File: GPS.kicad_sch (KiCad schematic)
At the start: 8 parts, among them J10 SMAConn, SW3 GPS_BattCheck, U7 MTK3339

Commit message: cleaner, still needs full checklisting
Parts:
- SW3: footprint Button_Switch_SMD:SW_SPST_B3SL-1002P -> UTSVT_Special:SW_SPST_B3SL-1002P
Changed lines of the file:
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@@
       (effects (font (size 1.27 1.27)) (justify left))
     )
-    (property "Footprint" "Button_Switch_SMD:SW_SPST_B3SL-1002P" (at 95.885 122.555 0)
+    (property "Footprint" "UTSVT_Special:SW_SPST_B3SL-1002P" (at 95.885 122.555 0)
       (effects (font (size 1.27 1.27)) hide)
     )

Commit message: neatening things up
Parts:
- J10: footprint Connector_Coaxial:SMA_Amphenol_132203-12_Horizontal -> UTSVT_Connectors:SMA_Amphenol_132203-12_Horizontal
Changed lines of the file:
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@@
       (effects (font (size 1.27 1.27)) (justify left))
     )
-    (property "Footprint" "Connector_Coaxial:SMA_Amphenol_132203-12_Horizontal" (at 192.405 98.425 0)
+    (property "Footprint" "UTSVT_Connectors:SMA_Amphenol_132203-12_Horizontal" (at 192.405 98.425 0)
       (effects (font (size 1.27 1.27)) hide)
     )

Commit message: bom, gerbers, edge cuts, footprint verification
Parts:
- BT2: P/N (none) -> 3000TR
- J10: P/N (none) -> 132203-12
- R26: P/N (none) -> CR0805-FX-5490ELF
- R27: P/N (none) -> CRCW0805750RFKEAHP
- U7: P/N (none) -> MTK3339
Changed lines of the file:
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@@
       (effects (font (size 1.27 1.27)) hide)
     )
-    (property "Datasheet" "~" (at 131.699 83.185 90)
+    (property "Datasheet" "https://www.mouser.com/datasheet/2/215/3000TR-742873.pdf" (at 131.699 83.185 90)
+      (effects (font (size 1.27 1.27)) hide)
+    )
+    (property "P/N" "3000TR" (at 130.175 83.185 0)
       (effects (font (size 1.27 1.27)) hide)
     )
@@
       (effects (font (size 1.27 1.27)) hide)
     )
-    (property "Datasheet" "~" (at 113.665 107.315 0)
+    (property "Datasheet" "https://www.mouser.com/datasheet/2/427/dcrcwe3-1762152.pdf" (at 113.665 107.315 0)
+      (effects (font (size 1.27 1.27)) hide)
+    )
+    (property "P/N" "CRCW0805750RFKEAHP" (at 113.665 107.315 0)
       (effects (font (size 1.27 1.27)) hide)
     )
@@
       (effects (font (size 1.27 1.27)) hide)
     )
-    (property "Datasheet" " ~" (at 192.405 98.425 0)
+    (property "Datasheet" "https://www.mouser.com/datasheet/2/18/1/amphs06488_1-2259725.pdf" (at 192.405 98.425 0)
+      (effects (font (size 1.27 1.27)) hide)
+    )
+    (property "P/N" "132203-12" (at 192.405 98.425 0)
       (effects (font (size 1.27 1.27)) hide)
     )
@@
     )
     (property "Datasheet" "https://www.mouser.com/ProductDetail/Adafruit/790?qs=sGAEpiMZZMu3sxpa5v1qro3UYtn2%252BmNbf7YcQf0l2Dw%3D" (at 168.275 73.025 0)
+      (effects (font (size 1.27 1.27)) hide)
+    )
+    (property "P/N" "MTK3339" (at 168.275 73.025 0)
       (effects (font (size 1.27 1.27)) hide)
     )
@@
       (effects (font (size 1.27 1.27)) hide)
     )
-    (property "Datasheet" "~" (at 90.805 107.315 0)
+    (property "Datasheet" "https://www.mouser.com/datasheet/2/54/cr-1858361.pdf" (at 90.805 107.315 0)
+      (effects (font (size 1.27 1.27)) hide)
+    )
+    (property "P/N" "CR0805-FX-5490ELF" (at 90.805 107.315 0)
       (effects (font (size 1.27 1.27)) hide)
     )
@@
       (effects (font (size 1.27 1.27)) hide)
     )
-    (property "Datasheet" "~" (at 95.885 122.555 0)
-      (effects (font (size 1.27 1.27)) hide)
-    )
+    (property "Datasheet" "https://www.mouser.com/datasheet/2/307/en-b3sl-1093544.pdf" (at 95.885 122.555 0)
+      (effects (font (size 1.27 1.27)) hide)
+    )

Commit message: basic inputs
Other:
- moved on the sheet: BT2, D3, D4, J10, R26, R27, SW3, U7

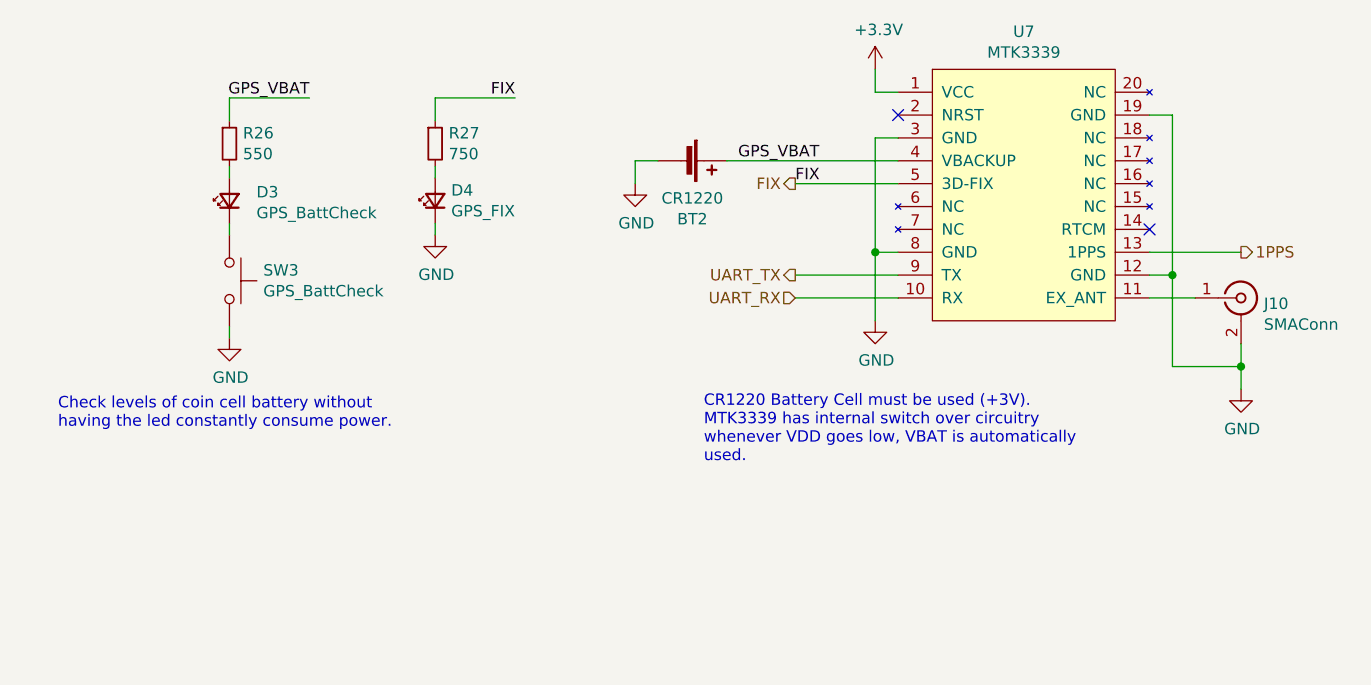
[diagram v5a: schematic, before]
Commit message: led fix + notes
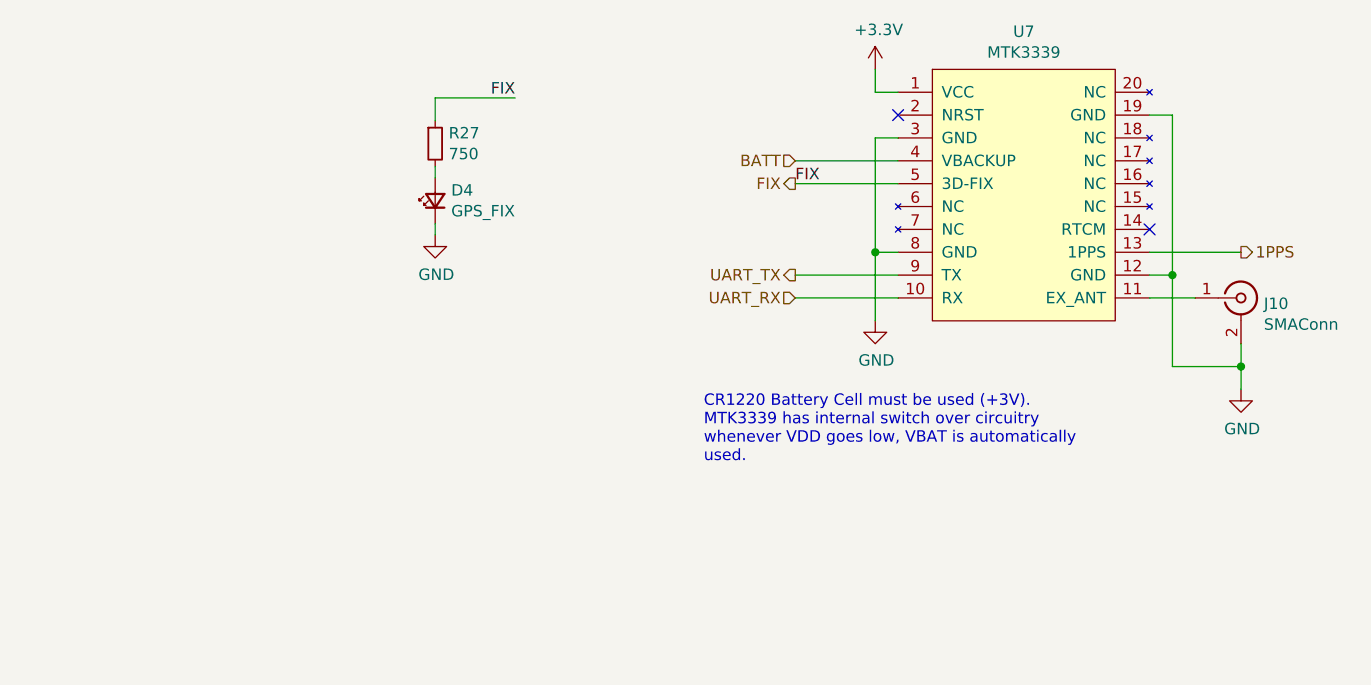
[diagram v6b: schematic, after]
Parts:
- removed BT2: CR1220, Battery:BatteryHolder_Keystone_3000_1x12mm, symbol Device:Battery_Cell
- removed D3: GPS_BattCheck, LED_SMD:LED_0805_2012Metric, symbol Device:LED_Small
- removed R26: 550, Resistor_SMD:R_0805_2012Metric, symbol Device:R_Small
- removed SW3: GPS_BattCheck, UTSVT_Special:SW_SPST_B3SL-1002P, symbol Switch:SW_Push
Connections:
- net GPS_VBAT renamed BATT
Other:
- note removed: "Check levels of coin cell battery without having the led constantly consume power."
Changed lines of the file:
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@@
-    (stroke (width 0) (type default))
-  )
-  (wire (pts (xy 95.25 101.6) (xy 95.25 102.87))
     (stroke (width 0) (type default))
   )
@@
     (stroke (width 0) (type default))
   )
-  (wire (pts (xy 95.25 85.09) (xy 95.25 83.82))
-    (stroke (width 0) (type default))
-  )
   (wire (pts (xy 118.11 76.2) (xy 127 76.2))
     (stroke (width 0) (type default))
@@
     (stroke (width 0) (type default))
   )
-  (wire (pts (xy 104.14 76.2) (xy 95.25 76.2))
-    (stroke (width 0) (type default))
-  )
   (wire (pts (xy 118.11 78.74) (xy 118.11 76.2))
     (stroke (width 0) (type default))
   )
-  (wire (pts (xy 140.335 83.185) (xy 142.875 83.185))
-    (stroke (width 0) (type default))
-  )
   (wire (pts (xy 167.005 93.345) (xy 167.005 80.645))
     (stroke (width 0) (type default))
@@
     (stroke (width 0) (type default))
   )
-  (wire (pts (xy 140.335 85.725) (xy 140.335 83.185))
-    (stroke (width 0) (type default))
-  )
   (wire (pts (xy 167.005 93.345) (xy 169.545 93.345))
     (stroke (width 0) (type default))
@@
     (stroke (width 0) (type default))
   )
-  (wire (pts (xy 150.495 83.185) (xy 169.545 83.185))
-    (stroke (width 0) (type default))
-  )
   (wire (pts (xy 197.485 98.425) (xy 202.565 98.425))
     (stroke (width 0) (type default))
@@
     (stroke (width 0) (type default))
   )
+  (wire (pts (xy 158.115 83.185) (xy 169.545 83.185))
+    (stroke (width 0) (type default))
+  )
   (wire (pts (xy 207.645 106.045) (xy 207.645 103.505))
     (stroke (width 0) (type default))
@@
     (stroke (width 0) (type default))
   )
-  (wire (pts (xy 95.25 91.44) (xy 95.25 90.17))
-    (stroke (width 0) (type default))
-  )
-  (wire (pts (xy 95.25 76.2) (xy 95.25 78.74))
-    (stroke (width 0) (type default))
-  )
   (wire (pts (xy 118.11 83.82) (xy 118.11 85.09))
     (stroke (width 0) (type default))
@@
   (wire (pts (xy 200.025 95.885) (xy 197.485 95.885))
     (stroke (width 0) (type default))
-  )
-  (text "Check levels of coin cell battery without\nhaving the led constantly consume power."
-    (at 76.2 113.03 0)
-    (effects (font (size 1.27 1.27)) (justify left bottom))
   )
   (text "CR1220 Battery Cell must be used (+3V).\nMTK3339 has internal switch over circuitry\nwhenever VDD goes low, VBAT is automatically\nused."
@@
     (effects (font (size 1.27 1.27)) (justify left bottom))
   )
-  (label "GPS_VBAT" (at 104.14 76.2 180) (fields_autoplaced)
-    (effects (font (size 1.27 1.27)) (justify right bottom))
-  )
   (label "FIX" (at 158.115 85.725 0) (fields_autoplaced)
     (effects (font (size 1.27 1.27)) (justify left bottom))
   )
-  (label "GPS_VBAT" (at 151.765 83.185 0) (fields_autoplaced)
-    (effects (font (size 1.27 1.27)) (justify left bottom))
-  )
   (label "FIX" (at 127 76.2 180) (fields_autoplaced)
     (effects (font (size 1.27 1.27)) (justify right bottom))
@@
     (effects (font (size 1.27 1.27)) (justify right))
   )
+  (hierarchical_label "BATT" (shape input) (at 158.115 83.185 180) (fields_autoplaced)
+    (effects (font (size 1.27 1.27)) (justify right))
+  )
   (hierarchical_label "1PPS" (shape output) (at 207.645 93.345 0) (fields_autoplaced)
     (effects (font (size 1.27 1.27)) (justify left))
@@
   (hierarchical_label "UART_RX" (shape input) (at 158.115 98.425 180) (fields_autoplaced)
     (effects (font (size 1.27 1.27)) (justify right))
-  )
-  (symbol (lib_id "Device:Battery_Cell") (at 145.415 83.185 270) (unit 1)
-    (in_bom yes) (on_board yes) (dnp no)
-    (property "Reference" "BT2" (at 146.685 89.662 90)
-      (effects (font (size 1.27 1.27)))
-    )
-    (property "Value" "CR1220" (at 146.685 87.3506 90)
-      (effects (font (size 1.27 1.27)))
-    )
-    (property "Footprint" "Battery:BatteryHolder_Keystone_3000_1x12mm" (at 146.939 83.185 90)
-      (effects (font (size 1.27 1.27)) hide)
-    )
-    (property "Datasheet" "https://www.mouser.com/datasheet/2/215/3000TR-742873.pdf" (at 146.939 83.185 90)
-      (effects (font (size 1.27 1.27)) hide)
-    )
-    (property "P/N" "3000TR" (at 145.415 83.185 0)
-      (effects (font (size 1.27 1.27)) hide)
-    )
-    (pin "1")
-    (pin "2")
-    (instances
-      (project "Telemetry-Primary"
-        (path "/7f2a449b-14af-42b3-8d38-5f0f8a5ee7ce/00000000-0000-0000-0000-00005f6efd51"
-          (reference "BT2") (unit 1)
-        )
-      )
-    )
-  )
-  (symbol (lib_id "power:GND") (at 140.335 85.725 0) (unit 1)
-    (in_bom yes) (on_board yes) (dnp no)
-    (property "Reference" "#PWR0157" (at 140.335 92.075 0)
-      (effects (font (size 1.27 1.27)) hide)
-    )
-    (property "Value" "GND" (at 140.462 90.1192 0)
-      (effects (font (size 1.27 1.27)))
-    )
-    (property "Footprint" "" (at 140.335 85.725 0)
-      (effects (font (size 1.27 1.27)) hide)
-    )
-    (property "Datasheet" "" (at 140.335 85.725 0)
-      (effects (font (size 1.27 1.27)) hide)
-    )
-    (pin "1")
-    (instances
-      (project "Telemetry-Primary"
-        (path "/7f2a449b-14af-42b3-8d38-5f0f8a5ee7ce/00000000-0000-0000-0000-00005f6efd51"
-          (reference "#PWR0157") (unit 1)
-        )
-      )
-    )
   )
   (symbol (lib_id "Device:LED_Small") (at 118.11 87.63 90) (unit 1)
@@
         )
       )
-    )
-  )
-  (symbol (lib_id "power:GND") (at 95.25 102.87 0) (unit 1)
-    (in_bom yes) (on_board yes) (dnp no)
-    (property "Reference" "#PWR0159" (at 95.25 109.22 0)
-      (effects (font (size 1.27 1.27)) hide)
-    )
-    (property "Value" "GND" (at 95.377 107.2642 0)
-      (effects (font (size 1.27 1.27)))
-    )
-    (property "Footprint" "" (at 95.25 102.87 0)
-      (effects (font (size 1.27 1.27)) hide)
-    )
-    (property "Datasheet" "" (at 95.25 102.87 0)
-      (effects (font (size 1.27 1.27)) hide)
-    )
-    (pin "1")
-    (instances
-      (project "Telemetry-Primary"
-        (path "/7f2a449b-14af-42b3-8d38-5f0f8a5ee7ce/00000000-0000-0000-0000-00005f6efd51"
-          (reference "#PWR0159") (unit 1)
-        )
-        (path "/7f2a449b-14af-42b3-8d38-5f0f8a5ee7ce/00000000-0000-0000-0000-00005f6cdfd6"
-          (reference "#PWR?") (unit 1)
-        )
-      )
-    )
-  )
-  (symbol (lib_id "Device:LED_Small") (at 95.25 87.63 90) (unit 1)
-    (in_bom yes) (on_board yes) (dnp no)
-    (property "Reference" "D3" (at 98.2472 86.6648 90)
-      (effects (font (size 1.27 1.27)) (justify right))
-    )
-    (property "Value" "GPS_BattCheck" (at 98.2472 88.9762 90)
-      (effects (font (size 1.27 1.27)) (justify right))
-    )
-    (property "Footprint" "LED_SMD:LED_0805_2012Metric" (at 95.25 87.63 0)
-      (effects (font (size 1.27 1.27)) hide)
-    )
-    (property "Datasheet" "https://www.mouser.com/datasheet/2/216/APTD2012LCGCK-1102037.pdf" (at 95.25 87.63 0)
-      (effects (font (size 1.27 1.27)) hide)
-    )
-    (property "Color" "Green" (at 95.25 87.63 90)
-      (effects (font (size 1.27 1.27)) hide)
-    )
-    (property "P/N" "APTD2012LCGCK" (at 95.25 87.63 90)
-      (effects (font (size 1.27 1.27)) hide)
-    )
-    (property "Vf" "1.9V" (at 95.25 87.63 90)
-      (effects (font (size 1.27 1.27)) hide)
-    )
-    (property "If" "2mA" (at 95.25 87.63 90)
-      (effects (font (size 1.27 1.27)) hide)
-    )
-    (pin "1")
-    (pin "2")
-    (instances
-      (project "Telemetry-Primary"
-        (path "/7f2a449b-14af-42b3-8d38-5f0f8a5ee7ce/00000000-0000-0000-0000-00005f6efd51"
-          (reference "D3") (unit 1)
-        )
-        (path "/7f2a449b-14af-42b3-8d38-5f0f8a5ee7ce/00000000-0000-0000-0000-00005f6cdfd6"
-          (reference "D?") (unit 1)
-        )
-      )
-    )
-  )
-  (symbol (lib_id "Device:R_Small") (at 95.25 81.28 0) (unit 1)
-    (in_bom yes) (on_board yes) (dnp no)
-    (property "Reference" "R26" (at 96.7486 80.1116 0)
-      (effects (font (size 1.27 1.27)) (justify left))
-    )
-    (property "Value" "550" (at 96.7486 82.423 0)
-      (effects (font (size 1.27 1.27)) (justify left))
-    )
-    (property "Footprint" "Resistor_SMD:R_0805_2012Metric" (at 95.25 81.28 0)
-      (effects (font (size 1.27 1.27)) hide)
-    )
-    (property "Datasheet" "https://www.mouser.com/datasheet/2/54/cr-1858361.pdf" (at 95.25 81.28 0)
-      (effects (font (size 1.27 1.27)) hide)
-    )
-    (property "P/N" "CR0805-FX-5490ELF" (at 95.25 81.28 0)
-      (effects (font (size 1.27 1.27)) hide)
-    )
-    (pin "1")
-    (pin "2")
-    (instances
-      (project "Telemetry-Primary"
-        (path "/7f2a449b-14af-42b3-8d38-5f0f8a5ee7ce/00000000-0000-0000-0000-00005f6efd51"
-          (reference "R26") (unit 1)
-        )
-      )
-    )
-  )
-  (symbol (lib_id "Switch:SW_Push") (at 95.25 96.52 270) (unit 1)
-    (in_bom yes) (on_board yes) (dnp no)
-    (property "Reference" "SW3" (at 99.0092 95.3516 90)
-      (effects (font (size 1.27 1.27)) (justify left))
-    )
-    (property "Value" "GPS_BattCheck" (at 99.0092 97.663 90)
-      (effects (font (size 1.27 1.27)) (justify left))
-    )
-    (property "Footprint" "UTSVT_Special:SW_SPST_B3SL-1002P" (at 100.33 96.52 0)
-      (effects (font (size 1.27 1.27)) hide)
-    )
-    (property "Datasheet" "https://www.mouser.com/datasheet/2/307/en-b3sl-1093544.pdf" (at 100.33 96.52 0)
-      (effects (font (size 1.27 1.27)) hide)
-    )
-    (property "P/N" "EVQ-7Q203W or B3SL-1002P" (at 95.25 96.52 90)
-      (effects (font (size 1.27 1.27)) hide)
-    )
-    (pin "1")
-    (pin "2")
-    (instances
-      (project "Telemetry-Primary"
-        (path "/7f2a449b-14af-42b3-8d38-5f0f8a5ee7ce/00000000-0000-0000-0000-00005f6efd51"
-          (reference "SW3") (unit 1)
-        )
-        (path "/7f2a449b-14af-42b3-8d38-5f0f8a5ee7ce"
-          (reference "SW?") (unit 1)
-        )
-      )

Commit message: inputs routing + fixed models + clock keepouts
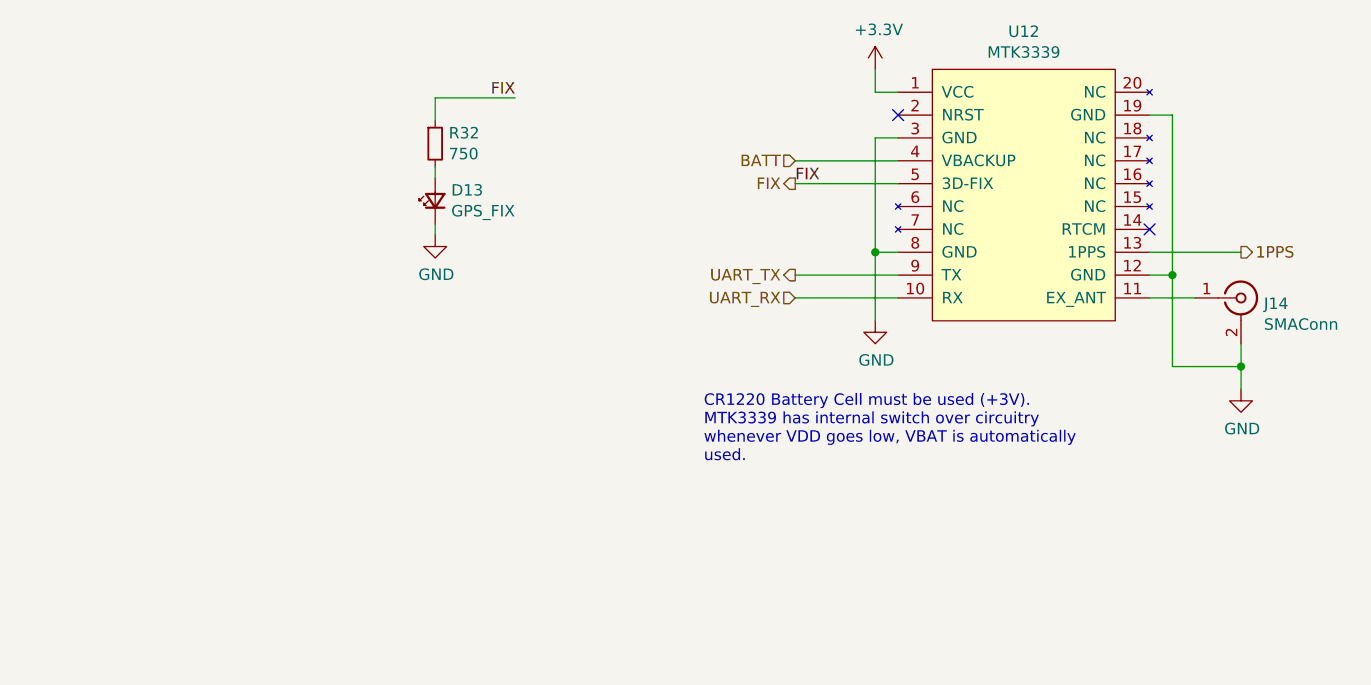
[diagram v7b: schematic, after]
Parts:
- renumbered D4 to D13, J10 to J14, R27 to R32, U7 to U12
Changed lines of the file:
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@@
   (symbol (lib_id "Device:LED_Small") (at 118.11 87.63 90) (unit 1)
     (in_bom yes) (on_board yes) (dnp no)
-    (property "Reference" "D4" (at 119.888 86.4616 90)
+    (property "Reference" "D13" (at 119.888 86.4616 90)
       (effects (font (size 1.27 1.27)) (justify right))
     )
@@
       (project "Telemetry-Primary"
         (path "/7f2a449b-14af-42b3-8d38-5f0f8a5ee7ce/00000000-0000-0000-0000-00005f6efd51"
-          (reference "D4") (unit 1)
+          (reference "D13") (unit 1)
         )
       )
@@
   (symbol (lib_id "Device:R_Small") (at 118.11 81.28 0) (unit 1)
     (in_bom yes) (on_board yes) (dnp no)
-    (property "Reference" "R27" (at 119.6086 80.1116 0)
+    (property "Reference" "R32" (at 119.6086 80.1116 0)
       (effects (font (size 1.27 1.27)) (justify left))
     )
@@
       (project "Telemetry-Primary"
         (path "/7f2a449b-14af-42b3-8d38-5f0f8a5ee7ce/00000000-0000-0000-0000-00005f6efd51"
-          (reference "R27") (unit 1)
+          (reference "R32") (unit 1)
         )
       )
@@
   (symbol (lib_id "Connector:Conn_Coaxial") (at 207.645 98.425 0) (unit 1)
     (in_bom yes) (on_board yes) (dnp no)
-    (property "Reference" "J10" (at 210.185 99.06 0)
+    (property "Reference" "J14" (at 210.185 99.06 0)
       (effects (font (size 1.27 1.27)) (justify left))
     )
@@
       (project "Telemetry-Primary"
         (path "/7f2a449b-14af-42b3-8d38-5f0f8a5ee7ce/00000000-0000-0000-0000-00005f6efd51"
-          (reference "J10") (unit 1)
+          (reference "J14") (unit 1)
         )
       )
@@
   (symbol (lib_id "utsvt-chips:MTK3339") (at 183.515 73.025 0) (unit 1)
     (in_bom yes) (on_board yes) (dnp no)
-    (property "Reference" "U7" (at 183.515 68.834 0)
+    (property "Reference" "U12" (at 183.515 68.834 0)
       (effects (font (size 1.27 1.27)))
     )
@@
       (project "Telemetry-Primary"
         (path "/7f2a449b-14af-42b3-8d38-5f0f8a5ee7ce/00000000-0000-0000-0000-00005f6efd51"
-          (reference "U7") (unit 1)
+          (reference "U12") (unit 1)
         )
       )
